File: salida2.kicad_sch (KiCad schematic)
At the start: 7 parts

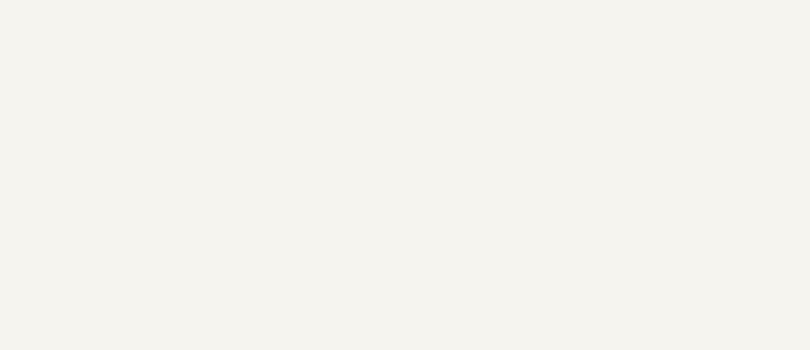
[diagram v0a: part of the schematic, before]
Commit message: add salidas separadas 4,5,6
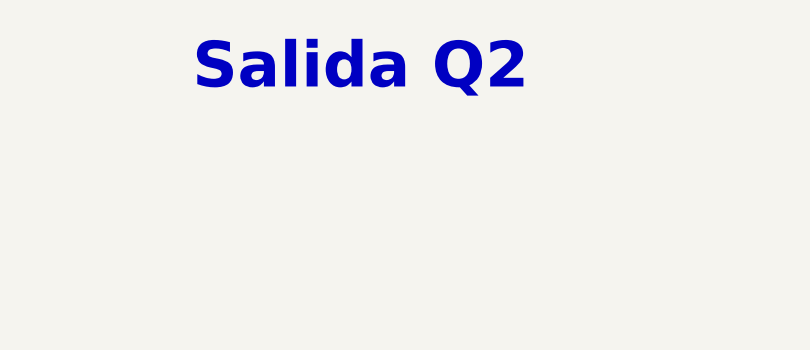
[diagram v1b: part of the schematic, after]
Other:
- note added: "Salida Q2"
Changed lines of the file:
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@@
     (stroke (width 0) (type default))
+  )
+  (text "Salida Q2" (at 86.36 81.28 0)
+    (effects (font (size 5.08 5.08) (thickness 1.016) bold) (justify left bottom))
   )
   (hierarchical_label "3L" (shape input) (at 148.59 115.57 0) (fields_autoplaced)

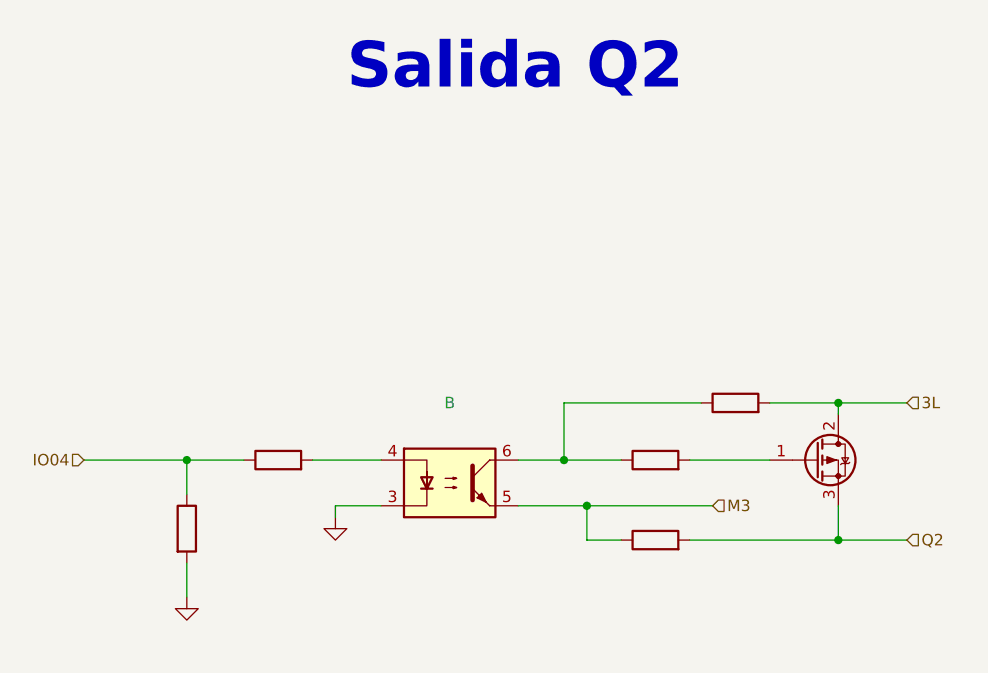
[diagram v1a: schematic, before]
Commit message: add entradas separadas
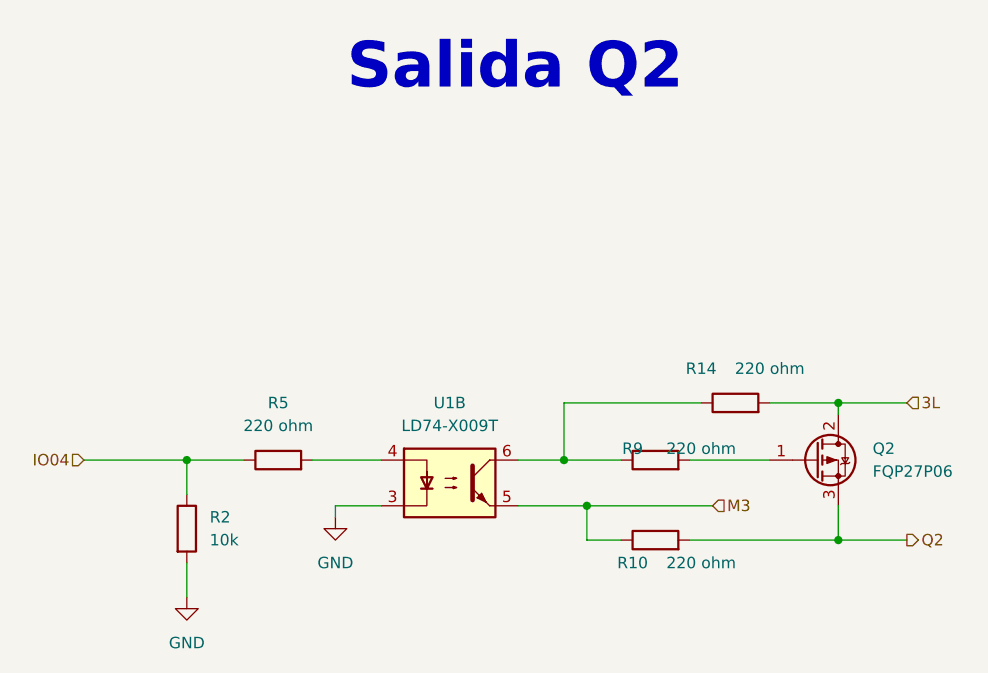
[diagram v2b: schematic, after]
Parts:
- Q2: renamed from ?; value (none) -> FQP27P06; footprint (none) -> Package_TO_SOT_SMD:TO-252-3_TabPin2
- R10, R14, R5, R9: renamed from ?; value (none) -> 220 ohm; footprint (none) -> Resistor_SMD:R_0603_1608Metric
- R2: renamed from ?; value (none) -> 10k; footprint (none) -> Resistor_SMD:R_0603_1608Metric
- U1: renamed from ?; value (none) -> LD74-X009T; footprint (none) -> Package_DIP:DIP-8_W8.89mm_SMDSocket_LongPads
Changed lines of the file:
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@@
-(kicad_sch (version 20220929) (generator eeschema)
+(kicad_sch (version 20221004) (generator eeschema)
   (paper "A4" portrait)
+  (title_block
+    (rev "José Luis Laica")
+  )
   (junction (at 140.97 115.57) (diameter 0) (color 0 0 0 0)
   )
@@
     (effects (font (size 1.27 1.27)) (justify right))
   )
-  (hierarchical_label "Q2" (shape input) (at 148.59 130.81 0) (fields_autoplaced)
+  (hierarchical_label "Q2" (shape output) (at 148.59 130.81 0) (fields_autoplaced)
     (effects (font (size 1.27 1.27)) (justify left))
   )
@@
   (symbol (lib_id "power:GND") (at 85.09 128.27 0) (unit 1)
     (in_bom yes) (on_board yes) (dnp no) (fields_autoplaced)
-    (default_instance (reference "") (unit 1) (value "") (footprint ""))
-    (property "Reference" "" (at 85.09 134.62 0)
-      (effects (font (size 1.27 1.27)) hide)
-    )
-    (property "Value" "" (at 85.09 133.35 0)
+    (property "Reference" "#PWR09" (at 85.09 134.62 0)
+      (effects (font (size 1.27 1.27)) hide)
+    )
+    (property "Value" "GND" (at 85.09 133.35 0)
       (effects (font (size 1.27 1.27)))
     )
@@
     )
     (pin "1")
+    (instances
+      (project "PLC 32 V2"
+        (path "/d17a54f1-6eda-453f-95e1-42a53b02a1c3/2637b07c-4b5f-4e3d-b3e5-25bd73194631"
+          (reference "#PWR09") (unit 1) (value "GND") (footprint "")
+        )
+      )
+    )
   )
   (symbol (lib_id "Transistor_FET:FQP27P06") (at 138.43 121.92 0) (unit 1)
     (in_bom yes) (on_board yes) (dnp no) (fields_autoplaced)
-    (default_instance (reference "") (unit 1) (value "") (footprint ""))
-    (property "Reference" "" (at 144.78 120.6499 0)
-      (effects (font (size 1.27 1.27)) (justify left))
-    )
-    (property "Value" "" (at 144.78 123.1899 0)
-      (effects (font (size 1.27 1.27)) (justify left))
-    )
-    (property "Footprint" "" (at 143.51 123.825 0)
+    (property "Reference" "Q2" (at 144.78 120.6499 0)
+      (effects (font (size 1.27 1.27)) (justify left))
+    )
+    (property "Value" "FQP27P06" (at 144.78 123.1899 0)
+      (effects (font (size 1.27 1.27)) (justify left))
+    )
+    (property "Footprint" "Package_TO_SOT_SMD:TO-252-3_TabPin2" (at 143.51 123.825 0)
       (effects (font (size 1.27 1.27) italic) (justify left) hide)
     )
@@
     (pin "2")
     (pin "3")
+    (instances
+      (project "PLC 32 V2"
+        (path "/d17a54f1-6eda-453f-95e1-42a53b02a1c3/2637b07c-4b5f-4e3d-b3e5-25bd73194631"
+          (reference "Q2") (unit 1) (value "FQP27P06") (footprint "Package_TO_SOT_SMD:TO-252-3_TabPin2")
+        )
+      )
+    )
   )
   (symbol (lib_id "Device:R") (at 120.65 130.81 90) (unit 1)
     (in_bom yes) (on_board yes) (dnp no)
-    (default_instance (reference "") (unit 1) (value "") (footprint ""))
-    (property "Reference" "" (at 118.11 133.35 90)
-      (effects (font (size 1.27 1.27)))
-    )
-    (property "Value" "" (at 125.73 133.35 90)
-      (effects (font (size 1.27 1.27)))
-    )
-    (property "Footprint" "" (at 120.65 132.588 90)
+    (property "Reference" "R10" (at 118.11 133.35 90)
+      (effects (font (size 1.27 1.27)))
+    )
+    (property "Value" "220 ohm" (at 125.73 133.35 90)
+      (effects (font (size 1.27 1.27)))
+    )
+    (property "Footprint" "Resistor_SMD:R_0603_1608Metric" (at 120.65 132.588 90)
       (effects (font (size 1.27 1.27)) hide)
     )
@@
     (pin "1")
     (pin "2")
+    (instances
+      (project "PLC 32 V2"
+        (path "/d17a54f1-6eda-453f-95e1-42a53b02a1c3/2637b07c-4b5f-4e3d-b3e5-25bd73194631"
+          (reference "R10") (unit 1) (value "220 ohm") (footprint "Resistor_SMD:R_0603_1608Metric")
+        )
+      )
+    )
   )
   (symbol (lib_id "Device:R") (at 68.58 129.54 0) (unit 1)
     (in_bom yes) (on_board yes) (dnp no) (fields_autoplaced)
-    (default_instance (reference "") (unit 1) (value "") (footprint ""))
-    (property "Reference" "" (at 71.12 128.2699 0)
-      (effects (font (size 1.27 1.27)) (justify left))
-    )
-    (property "Value" "" (at 71.12 130.8099 0)
-      (effects (font (size 1.27 1.27)) (justify left))
-    )
-    (property "Footprint" "" (at 66.802 129.54 90)
+    (property "Reference" "R2" (at 71.12 128.2699 0)
+      (effects (font (size 1.27 1.27)) (justify left))
+    )
+    (property "Value" "10k" (at 71.12 130.8099 0)
+      (effects (font (size 1.27 1.27)) (justify left))
+    )
+    (property "Footprint" "Resistor_SMD:R_0603_1608Metric" (at 66.802 129.54 90)
       (effects (font (size 1.27 1.27)) hide)
     )
@@
     (pin "1")
     (pin "2")
+    (instances
+      (project "PLC 32 V2"
+        (path "/d17a54f1-6eda-453f-95e1-42a53b02a1c3/2637b07c-4b5f-4e3d-b3e5-25bd73194631"
+          (reference "R2") (unit 1) (value "10k") (footprint "Resistor_SMD:R_0603_1608Metric")
+        )
+      )
+    )
   )
   (symbol (lib_id "Device:R") (at 129.54 115.57 90) (unit 1)
     (in_bom yes) (on_board yes) (dnp no)
-    (default_instance (reference "") (unit 1) (value "") (footprint ""))
-    (property "Reference" "" (at 125.73 111.76 90)
-      (effects (font (size 1.27 1.27)))
-    )
-    (property "Value" "" (at 133.35 111.76 90)
-      (effects (font (size 1.27 1.27)))
-    )
-    (property "Footprint" "" (at 129.54 117.348 90)
+    (property "Reference" "R14" (at 125.73 111.76 90)
+      (effects (font (size 1.27 1.27)))
+    )
+    (property "Value" "220 ohm" (at 133.35 111.76 90)
+      (effects (font (size 1.27 1.27)))
+    )
+    (property "Footprint" "Resistor_SMD:R_0603_1608Metric" (at 129.54 117.348 90)
       (effects (font (size 1.27 1.27)) hide)
     )
@@
     (pin "1")
     (pin "2")
+    (instances
+      (project "PLC 32 V2"
+        (path "/d17a54f1-6eda-453f-95e1-42a53b02a1c3/2637b07c-4b5f-4e3d-b3e5-25bd73194631"
+          (reference "R14") (unit 1) (value "220 ohm") (footprint "Resistor_SMD:R_0603_1608Metric")
+        )
+      )
+    )
   )
   (symbol (lib_id "Device:R") (at 78.74 121.92 90) (unit 1)
     (in_bom yes) (on_board yes) (dnp no) (fields_autoplaced)
-    (default_instance (reference "") (unit 1) (value "") (footprint ""))
-    (property "Reference" "" (at 78.74 115.57 90)
-      (effects (font (size 1.27 1.27)))
-    )
-    (property "Value" "" (at 78.74 118.11 90)
-      (effects (font (size 1.27 1.27)))
-    )
-    (property "Footprint" "" (at 78.74 123.698 90)
+    (property "Reference" "R5" (at 78.74 115.57 90)
+      (effects (font (size 1.27 1.27)))
+    )
+    (property "Value" "220 ohm" (at 78.74 118.11 90)
+      (effects (font (size 1.27 1.27)))
+    )
+    (property "Footprint" "Resistor_SMD:R_0603_1608Metric" (at 78.74 123.698 90)
       (effects (font (size 1.27 1.27)) hide)
     )
@@
     (pin "1")
     (pin "2")
+    (instances
+      (project "PLC 32 V2"
+        (path "/d17a54f1-6eda-453f-95e1-42a53b02a1c3/2637b07c-4b5f-4e3d-b3e5-25bd73194631"
+          (reference "R5") (unit 1) (value "220 ohm") (footprint "Resistor_SMD:R_0603_1608Metric")
+        )
+      )
+    )
   )
   (symbol (lib_id "Isolator:ILD74") (at 97.79 124.46 0) (unit 2)
     (in_bom yes) (on_board yes) (dnp no) (fields_autoplaced)
-    (default_instance (reference "") (unit 1) (value "") (footprint ""))
-    (property "Reference" "" (at 97.79 115.57 0)
-      (effects (font (size 1.27 1.27)))
-    )
-    (property "Value" "" (at 97.79 118.11 0)
-      (effects (font (size 1.27 1.27)))
-    )
-    (property "Footprint" "" (at 92.71 129.54 0)
+    (property "Reference" "U1" (at 97.79 115.57 0)
+      (effects (font (size 1.27 1.27)))
+    )
+    (property "Value" "LD74-X009T" (at 97.79 118.11 0)
+      (effects (font (size 1.27 1.27)))
+    )
+    (property "Footprint" "Package_DIP:DIP-8_W8.89mm_SMDSocket_LongPads" (at 92.71 129.54 0)
       (effects (font (size 1.27 1.27) italic) (justify left) hide)
     )
@@
     (pin "5")
     (pin "6")
+    (instances
+      (project "PLC 32 V2"
+        (path "/d17a54f1-6eda-453f-95e1-42a53b02a1c3/2637b07c-4b5f-4e3d-b3e5-25bd73194631"
+          (reference "U1") (unit 2) (value "LD74-X009T") (footprint "Package_DIP:DIP-8_W8.89mm_SMDSocket_LongPads")
+        )
+      )
+    )
   )
   (symbol (lib_id "Device:R") (at 120.65 121.92 90) (unit 1)
     (in_bom yes) (on_board yes) (dnp no)
-    (default_instance (reference "") (unit 1) (value "") (footprint ""))
-    (property "Reference" "" (at 118.11 120.65 90)
-      (effects (font (size 1.27 1.27)))
-    )
-    (property "Value" "" (at 125.73 120.65 90)
-      (effects (font (size 1.27 1.27)))
-    )
-    (property "Footprint" "" (at 120.65 123.698 90)
+    (property "Reference" "R9" (at 118.11 120.65 90)
+      (effects (font (size 1.27 1.27)))
+    )
+    (property "Value" "220 ohm" (at 125.73 120.65 90)
+      (effects (font (size 1.27 1.27)))
+    )
+    (property "Footprint" "Resistor_SMD:R_0603_1608Metric" (at 120.65 123.698 90)
       (effects (font (size 1.27 1.27)) hide)
     )
@@
     (pin "1")
     (pin "2")
+    (instances
+      (project "PLC 32 V2"
+        (path "/d17a54f1-6eda-453f-95e1-42a53b02a1c3/2637b07c-4b5f-4e3d-b3e5-25bd73194631"
+          (reference "R9") (unit 1) (value "220 ohm") (footprint "Resistor_SMD:R_0603_1608Metric")
+        )
+      )
+    )
   )
   (symbol (lib_id "power:GND") (at 68.58 137.16 0) (unit 1)
     (in_bom yes) (on_board yes) (dnp no) (fields_autoplaced)
-    (default_instance (reference "") (unit 1) (value "") (footprint ""))
-    (property "Reference" "" (at 68.58 143.51 0)
-      (effects (font (size 1.27 1.27)) hide)
-    )
-    (property "Value" "" (at 68.58 142.24 0)
+    (property "Reference" "#PWR06" (at 68.58 143.51 0)
+      (effects (font (size 1.27 1.27)) hide)
+    )
+    (property "Value" "GND" (at 68.58 142.24 0)
       (effects (font (size 1.27 1.27)))
     )
@@
     )
     (pin "1")
+    (instances
+      (project "PLC 32 V2"
+        (path "/d17a54f1-6eda-453f-95e1-42a53b02a1c3/2637b07c-4b5f-4e3d-b3e5-25bd73194631"
+          (reference "#PWR06") (unit 1) (value "GND") (footprint "")
+        )
+      )
+    )
   )
 )

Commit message: input/output separadas
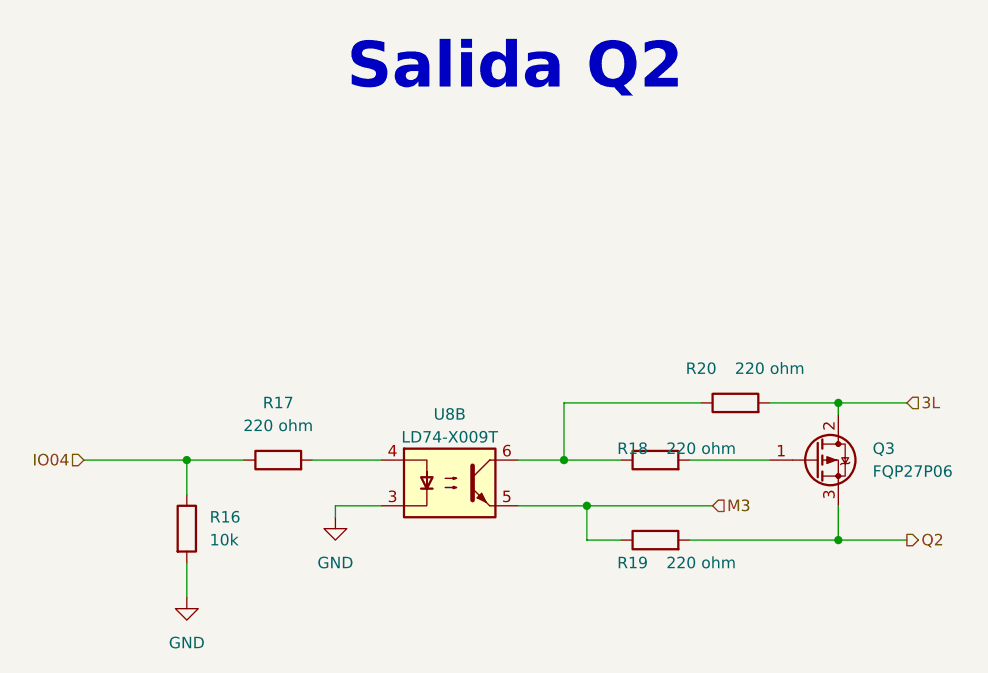
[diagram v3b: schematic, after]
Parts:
- renumbered Q2 to Q3, R2 to R16, R5 to R17, R9 to R18, R10 to R19, R14 to R20, U1 to U8
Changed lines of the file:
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@@
   (paper "A4" portrait)
   (title_block
+    (date "2022-10-09")
     (rev "José Luis Laica")
   )
@@
   (symbol (lib_id "power:GND") (at 85.09 128.27 0) (unit 1)
     (in_bom yes) (on_board yes) (dnp no) (fields_autoplaced)
-    (property "Reference" "#PWR09" (at 85.09 134.62 0)
+    (property "Reference" "#PWR015" (at 85.09 134.62 0)
       (effects (font (size 1.27 1.27)) hide)
     )
@@
       (project "PLC 32 V2"
         (path "/d17a54f1-6eda-453f-95e1-42a53b02a1c3/2637b07c-4b5f-4e3d-b3e5-25bd73194631"
-          (reference "#PWR09") (unit 1) (value "GND") (footprint "")
+          (reference "#PWR015") (unit 1) (value "GND") (footprint "")
         )
       )
@@
   (symbol (lib_id "Transistor_FET:FQP27P06") (at 138.43 121.92 0) (unit 1)
     (in_bom yes) (on_board yes) (dnp no) (fields_autoplaced)
-    (property "Reference" "Q2" (at 144.78 120.6499 0)
+    (property "Reference" "Q3" (at 144.78 120.6499 0)
       (effects (font (size 1.27 1.27)) (justify left))
     )
@@
       (project "PLC 32 V2"
         (path "/d17a54f1-6eda-453f-95e1-42a53b02a1c3/2637b07c-4b5f-4e3d-b3e5-25bd73194631"
-          (reference "Q2") (unit 1) (value "FQP27P06") (footprint "Package_TO_SOT_SMD:TO-252-3_TabPin2")
+          (reference "Q3") (unit 1) (value "FQP27P06") (footprint "Package_TO_SOT_SMD:TO-252-3_TabPin2")
         )
       )
@@
   (symbol (lib_id "Device:R") (at 120.65 130.81 90) (unit 1)
     (in_bom yes) (on_board yes) (dnp no)
-    (property "Reference" "R10" (at 118.11 133.35 90)
+    (property "Reference" "R19" (at 118.11 133.35 90)
       (effects (font (size 1.27 1.27)))
     )
@@
       (project "PLC 32 V2"
         (path "/d17a54f1-6eda-453f-95e1-42a53b02a1c3/2637b07c-4b5f-4e3d-b3e5-25bd73194631"
-          (reference "R10") (unit 1) (value "220 ohm") (footprint "Resistor_SMD:R_0603_1608Metric")
+          (reference "R19") (unit 1) (value "220 ohm") (footprint "Resistor_SMD:R_0603_1608Metric")
         )
       )
@@
   (symbol (lib_id "Device:R") (at 68.58 129.54 0) (unit 1)
     (in_bom yes) (on_board yes) (dnp no) (fields_autoplaced)
-    (property "Reference" "R2" (at 71.12 128.2699 0)
+    (property "Reference" "R16" (at 71.12 128.2699 0)
       (effects (font (size 1.27 1.27)) (justify left))
     )
@@
       (project "PLC 32 V2"
         (path "/d17a54f1-6eda-453f-95e1-42a53b02a1c3/2637b07c-4b5f-4e3d-b3e5-25bd73194631"
-          (reference "R2") (unit 1) (value "10k") (footprint "Resistor_SMD:R_0603_1608Metric")
+          (reference "R16") (unit 1) (value "10k") (footprint "Resistor_SMD:R_0603_1608Metric")
         )
       )
@@
   (symbol (lib_id "Device:R") (at 129.54 115.57 90) (unit 1)
     (in_bom yes) (on_board yes) (dnp no)
-    (property "Reference" "R14" (at 125.73 111.76 90)
+    (property "Reference" "R20" (at 125.73 111.76 90)
       (effects (font (size 1.27 1.27)))
     )
@@
       (project "PLC 32 V2"
         (path "/d17a54f1-6eda-453f-95e1-42a53b02a1c3/2637b07c-4b5f-4e3d-b3e5-25bd73194631"
-          (reference "R14") (unit 1) (value "220 ohm") (footprint "Resistor_SMD:R_0603_1608Metric")
+          (reference "R20") (unit 1) (value "220 ohm") (footprint "Resistor_SMD:R_0603_1608Metric")
         )
       )
@@
   (symbol (lib_id "Device:R") (at 78.74 121.92 90) (unit 1)
     (in_bom yes) (on_board yes) (dnp no) (fields_autoplaced)
-    (property "Reference" "R5" (at 78.74 115.57 90)
+    (property "Reference" "R17" (at 78.74 115.57 90)
       (effects (font (size 1.27 1.27)))
     )
@@
       (project "PLC 32 V2"
         (path "/d17a54f1-6eda-453f-95e1-42a53b02a1c3/2637b07c-4b5f-4e3d-b3e5-25bd73194631"
-          (reference "R5") (unit 1) (value "220 ohm") (footprint "Resistor_SMD:R_0603_1608Metric")
+          (reference "R17") (unit 1) (value "220 ohm") (footprint "Resistor_SMD:R_0603_1608Metric")
         )
       )
@@
   (symbol (lib_id "Isolator:ILD74") (at 97.79 124.46 0) (unit 2)
     (in_bom yes) (on_board yes) (dnp no) (fields_autoplaced)
-    (property "Reference" "U1" (at 97.79 115.57 0)
-      (effects (font (size 1.27 1.27)))
-    )
-    (property "Value" "LD74-X009T" (at 97.79 118.11 0)
+    (property "Reference" "U8" (at 97.79 116.84 0)
+      (effects (font (size 1.27 1.27)))
+    )
+    (property "Value" "LD74-X009T" (at 97.79 119.38 0)
       (effects (font (size 1.27 1.27)))
     )
@@
       (project "PLC 32 V2"
         (path "/d17a54f1-6eda-453f-95e1-42a53b02a1c3/2637b07c-4b5f-4e3d-b3e5-25bd73194631"
-          (reference "U1") (unit 2) (value "LD74-X009T") (footprint "Package_DIP:DIP-8_W8.89mm_SMDSocket_LongPads")
+          (reference "U8") (unit 2) (value "LD74-X009T") (footprint "Package_DIP:DIP-8_W8.89mm_SMDSocket_LongPads")
         )
       )
@@
   (symbol (lib_id "Device:R") (at 120.65 121.92 90) (unit 1)
     (in_bom yes) (on_board yes) (dnp no)
-    (property "Reference" "R9" (at 118.11 120.65 90)
+    (property "Reference" "R18" (at 118.11 120.65 90)
       (effects (font (size 1.27 1.27)))
     )
@@
       (project "PLC 32 V2"
         (path "/d17a54f1-6eda-453f-95e1-42a53b02a1c3/2637b07c-4b5f-4e3d-b3e5-25bd73194631"
-          (reference "R9") (unit 1) (value "220 ohm") (footprint "Resistor_SMD:R_0603_1608Metric")
+          (reference "R18") (unit 1) (value "220 ohm") (footprint "Resistor_SMD:R_0603_1608Metric")
         )
       )
@@
   (symbol (lib_id "power:GND") (at 68.58 137.16 0) (unit 1)
     (in_bom yes) (on_board yes) (dnp no) (fields_autoplaced)
-    (property "Reference" "#PWR06" (at 68.58 143.51 0)
+    (property "Reference" "#PWR014" (at 68.58 143.51 0)
       (effects (font (size 1.27 1.27)) hide)
     )
@@
       (project "PLC 32 V2"
         (path "/d17a54f1-6eda-453f-95e1-42a53b02a1c3/2637b07c-4b5f-4e3d-b3e5-25bd73194631"
-          (reference "#PWR06") (unit 1) (value "GND") (footprint "")
-        )
-      )
+          (reference "#PWR014") (unit 1) (value "GND") (footprint "")
+        )
+      )
